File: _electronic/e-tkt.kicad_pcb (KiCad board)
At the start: 4 copper layers, 99.6 x 76.2 mm, 110 parts

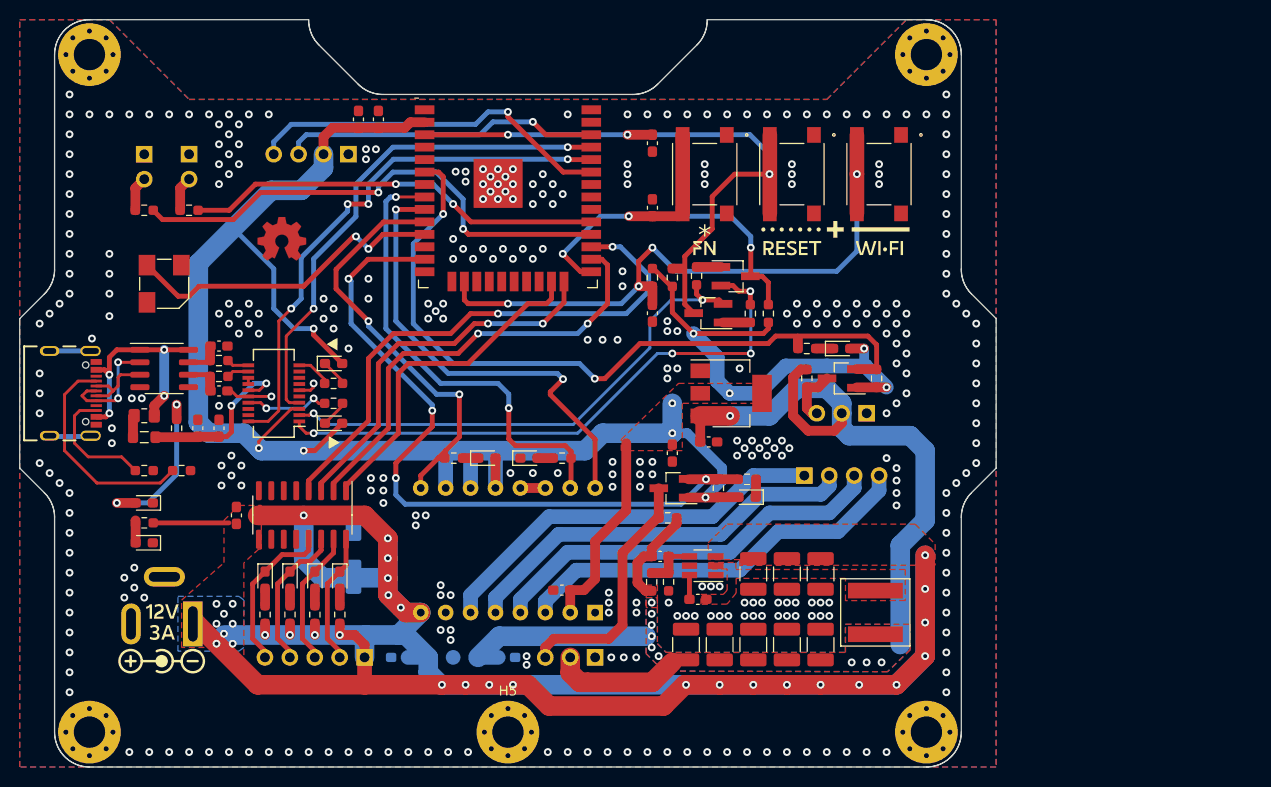
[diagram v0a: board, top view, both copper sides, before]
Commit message: BETA first upload
nothing major done here:
* updated KiCAD files to v9
* removed alternative 6v feed-in. The proposed buck converter is fine.
* added to all components LCSC component IDs. With this, exporting the project as gerber files also automatically creates correct BOM for JLCPCB manufacturing
*
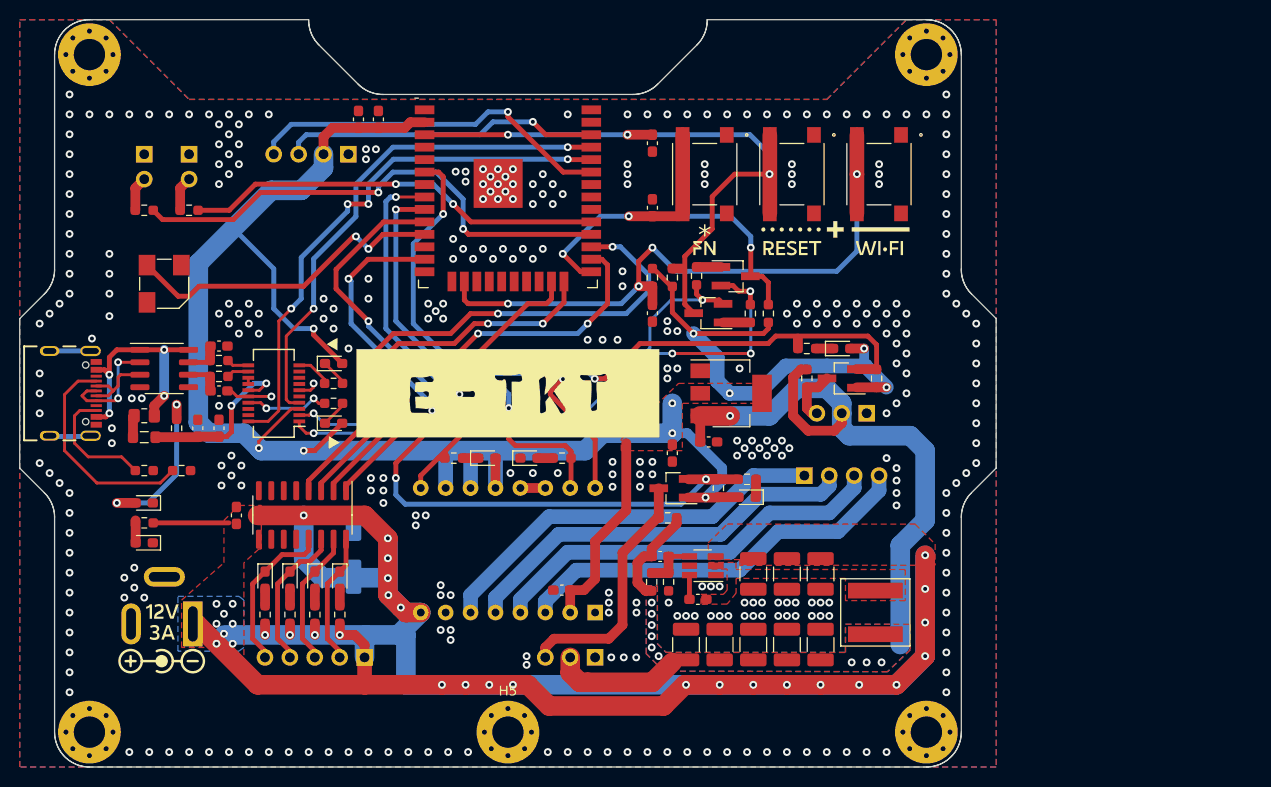
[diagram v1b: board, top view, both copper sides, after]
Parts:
- removed C_ALT6V_1: 0.33uF 50V, Capacitor_SMD:C_0603_1608Metric_Pad1.08x0.95mm_HandSolder
- removed C_ALT6V_2: 0.1uF 50V, Capacitor_SMD:C_0603_1608Metric_Pad1.08x0.95mm_HandSolder
- removed J_12v_ALT6V1, J_6v_ALT6V1, J_GND_ALT6V1: TestPoint, TestPoint:TestPoint_Pad_D1.5mm
- removed REF**: OSHW-Symbol_6.7x6mm_SilkScreen, andrei custom:opengear_small
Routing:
- net +6V: track 108.1 -> 88.0 mm

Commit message: Added CAD, cleaned up KiCAD some more
Added a FreeCAD Assembly. This will serve for minor updated to the printable parts.
Updated USB-C component to standard KiCAD libary-integrated version, because the pinout of the schematic symbol was messing with the pinout of the footprint
exported the PCB as step so it could be imported to FreeCAD
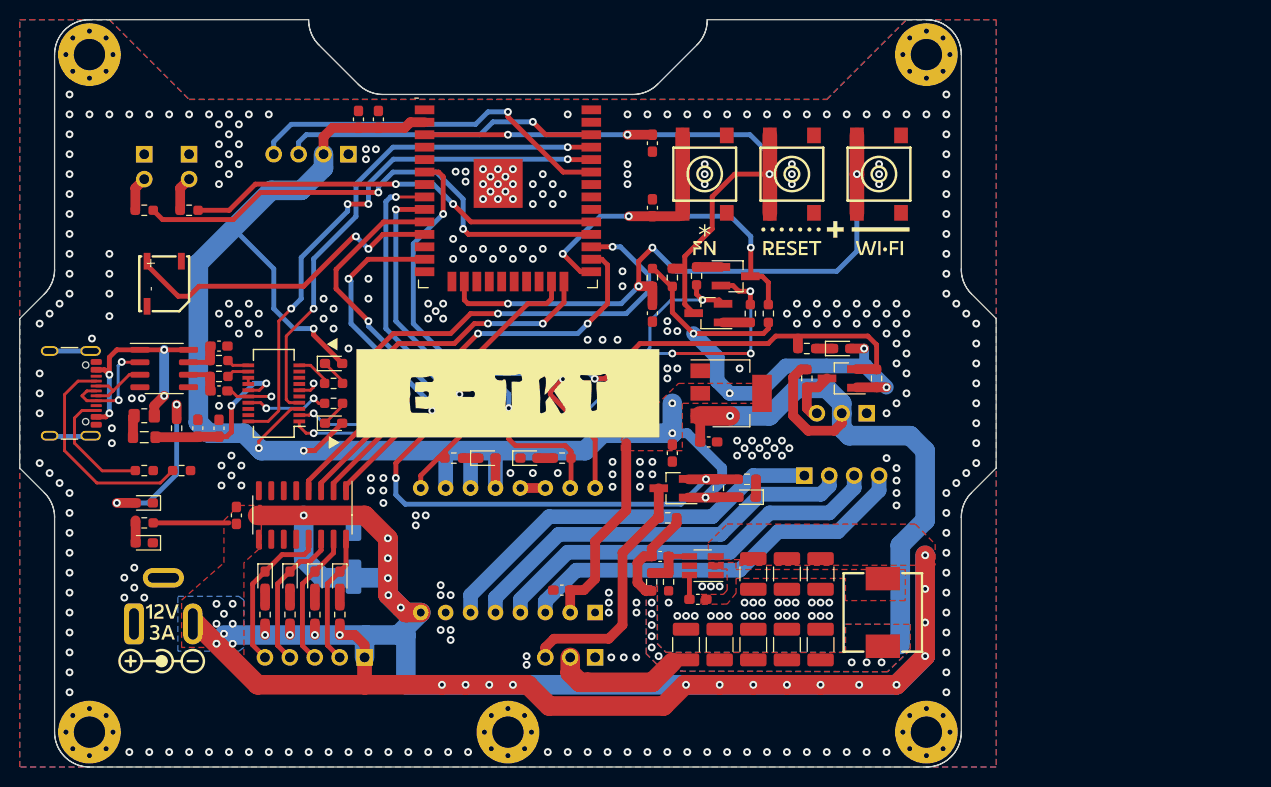
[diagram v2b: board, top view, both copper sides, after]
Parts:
- J_POW1: footprint SnapEDA Library:BarrelJack_GCT_DCJ200-10-A_Horizontal -> EASYEDA2KICAD:BarrelJack_Horizontal
- J_USB1: value USB4105-GF-A -> USB_C_Receptacle_USB2.0_16P; footprint SnapEDA Library:GCT_USB4105-GF-A -> Connector_USB:USB_C_Receptacle_GCT_USB4105-xx-A_16P_TopMnt_Horizontal
- L1: footprint SRP6060FA:SRP6060FA-4R7M -> EASYEDA2KICAD:IND-SMD_L8.5-W8.0_PSPMAA0803H-330M-ANP
- LS1: footprint SnapEDA Library:CUI_CSS-0575A-SMT -> EASYEDA2KICAD:BUZ-SMD_L5.0-W5.5-P4.60
- SW_DFU1, SW_ENA1, SW_WIFI1: footprint b3fs:B3FS-1000 -> EASYEDA2KICAD:KEY-SMD_4P-L6.0-W6.3-P4.50-LS8.0
- moved J_USB1 1.07 mm to (132.6, -189.5)
- moved L1 0.76 mm to (216.5, -167.1)
- turned J_POW1 to 0 degrees
- turned SW_DFU1 to 90 degrees
- turned SW_ENA1 to 90 degrees
- turned SW_WIFI1 to 90 degrees
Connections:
- net /USB-C 2.0/USBD1+ renamed Net-(J_USB1-D+-PadA6)
- net /USB-C 2.0/USBD1- renamed Net-(J_USB1-D--PadA7)
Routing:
- net Net-(J_USB1-D--PadA7): track 7.09 -> 6.57 mm

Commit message: Updated A_bottom in FreeCAD
added pockets for M3 nuts, added pockets for electronics cover

started to optimize pcb footprint layout and voltage reference planes
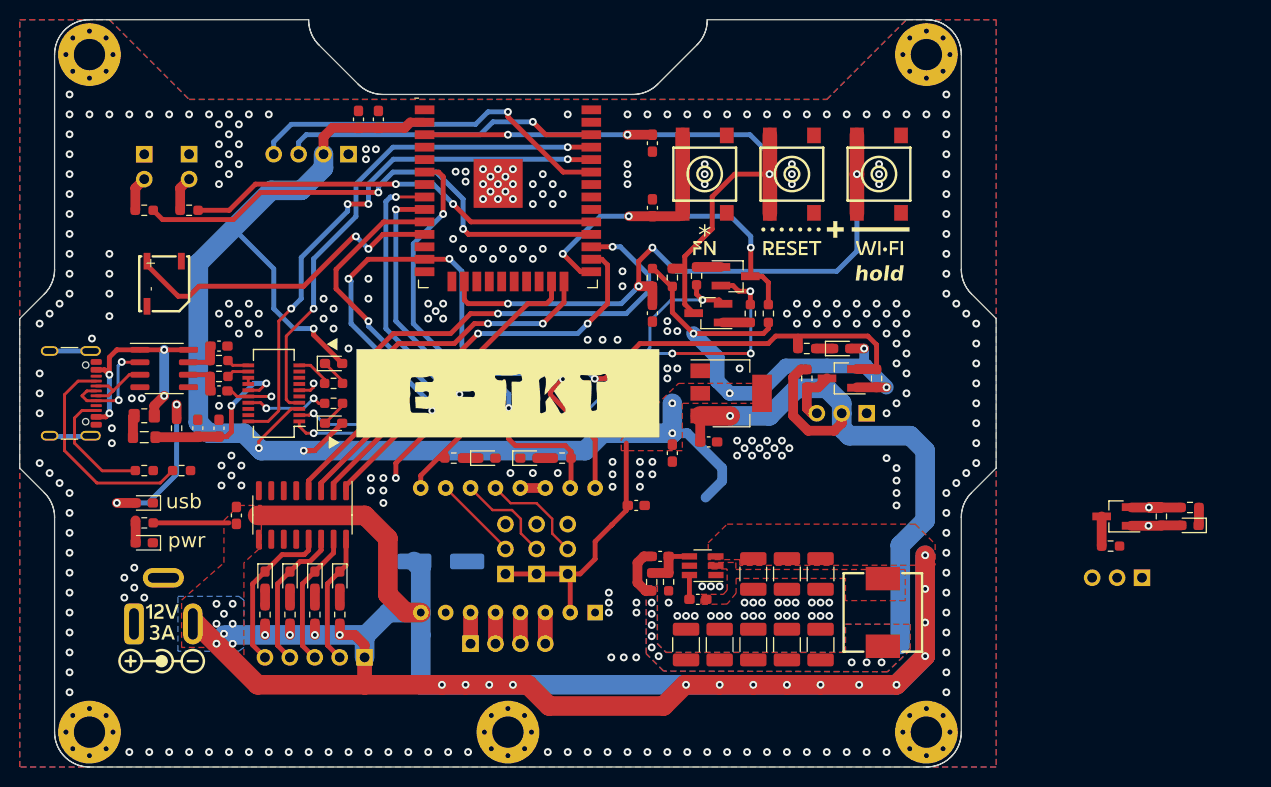
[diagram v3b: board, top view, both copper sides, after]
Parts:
- added J1: Conn_01x03_Pin, Connector_PinHeader_2.54mm:PinHeader_1x03_P2.54mm_Vertical, B.Cu at (178.1, -171.1)
- added J2: Conn_01x03_Pin, Connector_PinHeader_2.54mm:PinHeader_1x03_P2.54mm_Vertical, B.Cu at (181.2, -171.1)
- added J3: Conn_01x03_Pin, Connector_PinHeader_2.54mm:PinHeader_1x03_P2.54mm_Vertical, B.Cu at (184.4, -171.1)
- J_NEMA1: footprint Connector_PinHeader_2.54mm:PinHeader_1x04_P2.54mm_Horizontal -> Connector_PinHeader_2.54mm:PinHeader_1x04_P2.54mm_Vertical
- moved J_SERVO1 56.4 mm to (243.0, -170.7)
- moved Q_SERVO1 45.3 mm to (240.4, -176.9)
- moved R_SERVO2 45.3 mm to (244.9, -176.9)
- moved D_SERVO1 45.3 mm to (247.9, -176.0)
- moved R_SERVO1 45.3 mm to (239.8, -173.9)
- moved R_SERVO3 45.3 mm to (247.9, -177.8)
- moved G*** 41.0 mm to (152.6, -221.2)
- moved J_NEMA1 38.1 mm to (174.5, -164.0)
- moved C_NEMA2 11.5 mm to (191.4, -178.1), turned to 180 degrees
- moved C_NEMA1 8.96 mm to (171.4, -172.3), turned to 0 degrees
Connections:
- A_NEMA1 pad 10: +3.3V -> Net-(A_NEMA1-MS1)
- A_NEMA1 pad 11: +3.3V -> Net-(A_NEMA1-MS2)
- A_NEMA1 pad 12: +3.3V -> Net-(A_NEMA1-MS3)
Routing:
- net Net-(A_NEMA1-1B): track 41.4 -> 3.18 mm
- net Net-(A_NEMA1-1A): track 41.3 -> 3.18 mm
- net Net-(A_NEMA1-2A): track 41.3 -> 3.18 mm
- net Net-(A_NEMA1-2B): track 40.9 -> 3.18 mm
- net IO14 SERVO: track 76.4 -> 53.5 mm, vias 4 -> 5
- net SERVO: track 25.4 -> 3.02 mm
- net +6V: track 88.0 -> 69.8 mm
- net +12V: track 251.2 -> 233.2 mm, vias 33 -> 27
- net Net-(A_NEMA1-MS3): track 0.00 -> 10.8 mm
- net Net-(A_NEMA1-MS2): track 0.00 -> 10.2 mm
- net Net-(A_NEMA1-MS1): track 0.00 -> 8.76 mm
- net +3.3V: track 231.2 -> 223.3 mm
- net GNDREF: vias 351 -> 339
- added copper zone on In2.Cu, net +3.3V
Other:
- board text added: "H"
- board text added: "L"
- board text added: "hold"
- board text added: "pwr"
- board text added: "usb"

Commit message: Minor adjustments of CAD and EDA
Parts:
- moved J_SERVO1 26.8 mm to (253.3, -195.4)
- moved R_WIFI1 23.0 mm to (211.6, -214.8), turned to -90 degrees
- moved C_WIFI1 21.6 mm to (211.6, -208.7), turned to -90 degrees
- moved R_SERVO1 21.0 mm to (251.0, -191.6), turned to 90 degrees
- moved R_DFU1 20.4 mm to (194.0, -214.9)
- moved D_SERVO1 20.1 mm to (244.5, -195.8), turned to 0 degrees
- moved R_SERVO2 17.3 mm to (244.5, -194.2), turned to 0 degrees
- moved Q_SERVO1 16.3 mm to (247.4, -191.6), turned to 0 degrees
- moved Q_HALL1 16.0 mm to (196.4, -191.4)
- moved R_HALL2 15.9 mm to (200.0, -191.4)
- moved R_ENA1 15.6 mm to (202.8, -214.8)
- moved R_SERVO3 14.4 mm to (243.6, -191.6), turned to -90 degrees
- moved R_HALL1 14.4 mm to (194.9, -187.4), turned to -90 degrees
- moved U_POW2 14.0 mm to (190.5, -180.3), turned to 90 degrees
- moved J_HALL1 11.9 mm to (202.9, -187.4)
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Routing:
- net +3.3V: track 223.3 -> 120.0 mm, vias 10 -> 13
- net +6V: track 69.8 -> 13.1 mm, vias 10 -> 17
- net IO34 HALL: track 75.9 -> 42.6 mm
- net IO14 SERVO: track 53.5 -> 37.5 mm, vias 5 -> 3
- net +12V: track 233.2 -> 227.7 mm, vias 27 -> 20
- net IO32 NEMA STEP: track 47.6 -> 42.7 mm
- net GNDREF: track 15.1 -> 19.3 mm, vias 339 -> 286
- net EN: track 69.7 -> 65.8 mm, vias 3 -> 2
- net DTR: track 61.0 -> 57.4 mm, vias 4 -> 2
- net SERVO: track 3.02 -> 0.00 mm
- net IO25 NEMA ENA: track 43.0 -> 45.8 mm
- net IO33 NEMA DIR: track 47.4 -> 45.4 mm
- net Net-(D_SERVO1-K): track 1.84 -> 0.00 mm
- net IO0 DFU: track 47.3 -> 45.6 mm
- net IO13 WIFI RST: track 66.9 -> 68.3 mm
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- removed copper zone on F.Cu, net +3.3V

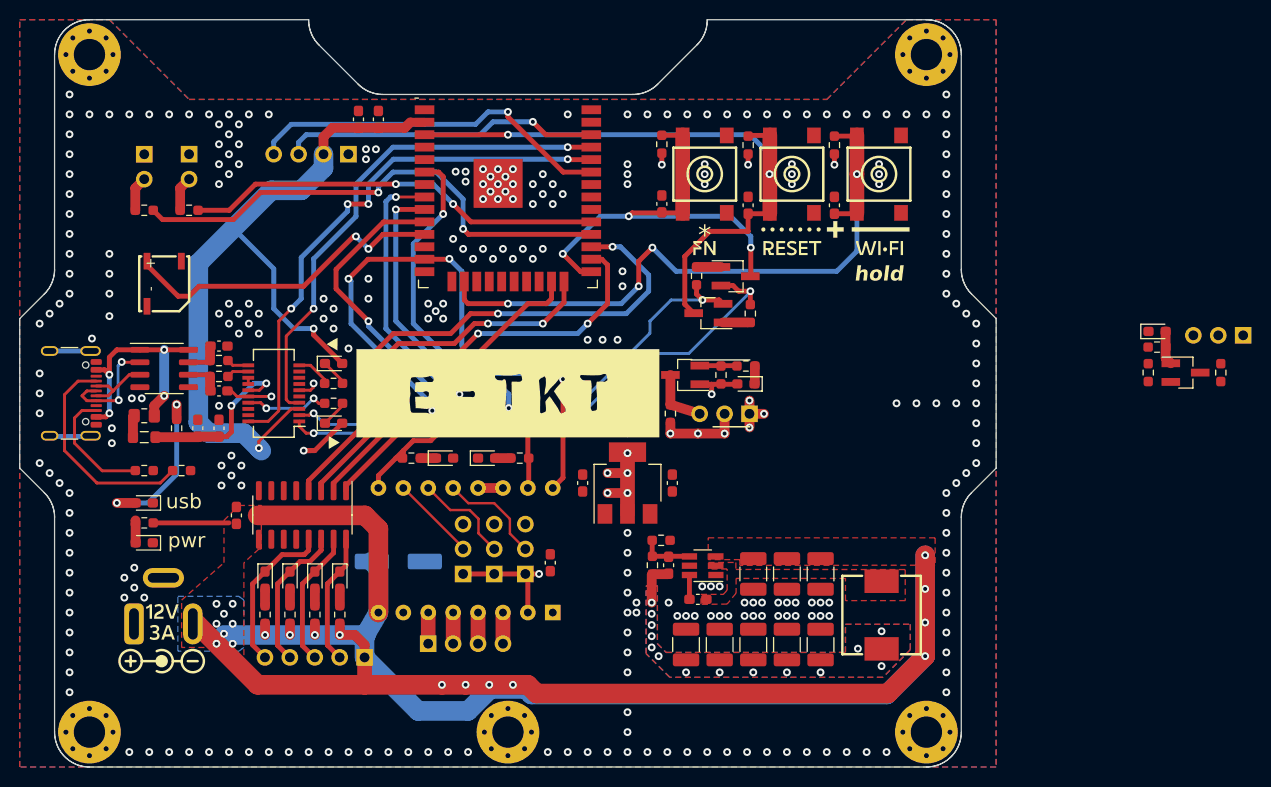
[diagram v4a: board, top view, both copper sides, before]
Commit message: Updating KiCAD files
some footprints in KicCAD v9 were updated versus v6 and threw warnings/errors. All footprints are now v9 compatible
wiring from ESP32 pins was optimized
layout of servo and hall level shift was optimized
layer 3 was split in 6V plane around the DCDC and 3V3 plane around everywhere else
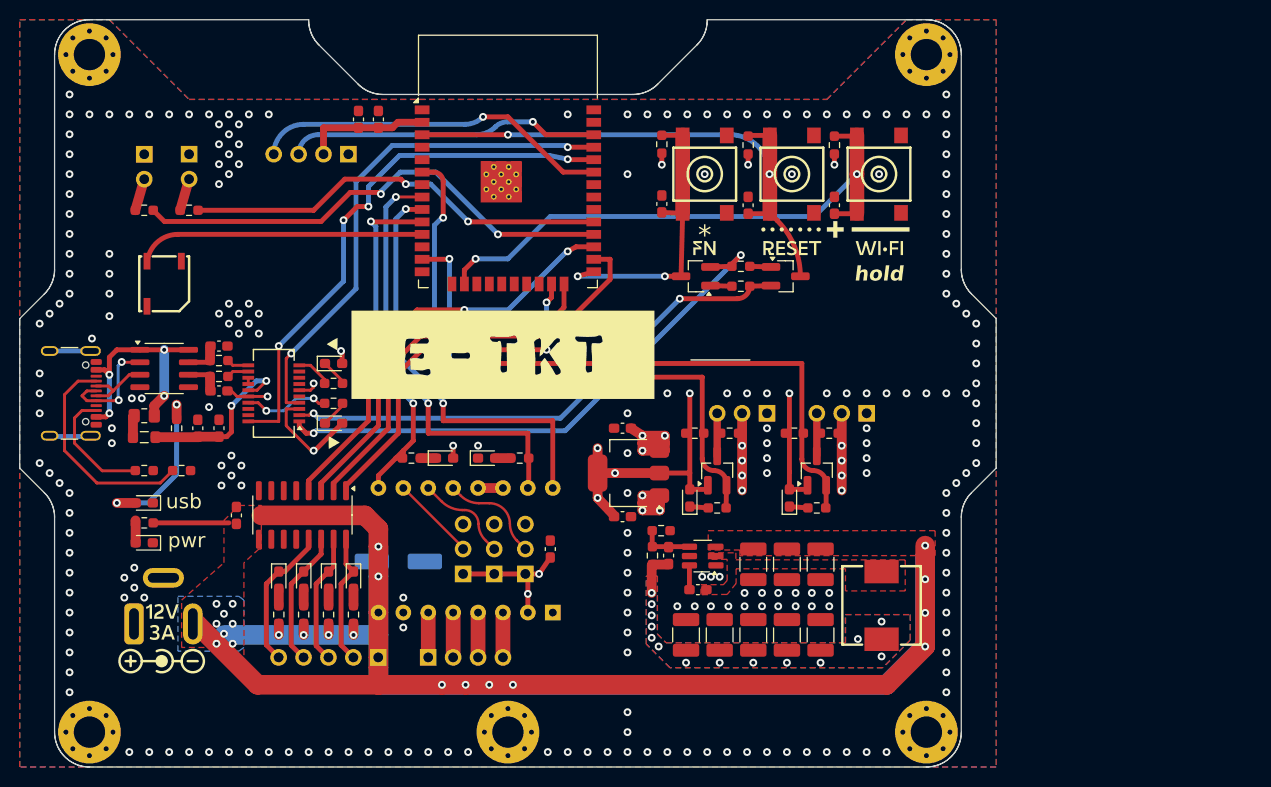
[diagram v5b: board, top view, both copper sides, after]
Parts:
- moved D_SERVO1 50.6 mm to (196.8, -178.8), turned to 90 degrees
- moved R_SERVO1 50.5 mm to (200.9, -185.4), turned to 0 degrees
- moved J_SERVO1 49.2 mm to (204.7, -187.5)
- moved Q_SERVO1 48.8 mm to (199.6, -181.6), turned to 90 degrees
- moved R_SERVO2 48.0 mm to (197.4, -185.4), turned to 180 degrees
- moved R_SERVO3 46.1 mm to (199.6, -177.8), turned to 180 degrees
- moved G*** 17.4 mm to (180.6, -206.2)
- moved Q_HALL1 16.6 mm to (209.8, -181.6), turned to 90 degrees
- moved R_HALL1 16.3 mm to (211.1, -185.4), turned to 0 degrees
- moved R_HALL3 16.2 mm to (209.8, -177.8), turned to 180 degrees
- moved D_HALL1 12.4 mm to (207.0, -178.8), turned to 90 degrees
- moved J_HALL1 11.9 mm to (214.9, -187.5)
- moved R_HALL2 9.55 mm to (207.5, -185.4), turned to 180 degrees
- moved Q_AUTO1 8.73 mm to (206.6, -201.4), turned to 0 degrees
- moved C_POW1 7.55 mm to (190.0, -185.9), turned to 180 degrees
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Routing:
- net +3.3V: track 120.0 -> 83.8 mm
- net IO34 HALL: track 42.6 -> 75.2 mm
- net +6V: track 13.1 -> 31.5 mm, vias 17 -> 25
- net IO14 SERVO: track 37.5 -> 55.0 mm, vias 3 -> 2
- net IO0 DFU: track 45.6 -> 31.4 mm, vias 3 -> 2
- net IO16 ULN 4: track 56.1 -> 43.4 mm
- net IO13 WIFI RST: track 68.3 -> 57.9 mm, vias 4 -> 2
- net EN: track 65.8 -> 56.9 mm
- net IO25 NEMA ENA: track 45.8 -> 37.4 mm
- net SERVO: track 0.00 -> 4.34 mm
- net GNDREF: track 19.3 -> 23.1 mm, vias 286 -> 233
- net /MCU/IO26 BUZZER OUT: track 33.3 -> 30.0 mm, vias 2 -> 0
- net IO15 ULN 1: track 34.7 -> 37.4 mm, vias 0 -> 2
- net RTS: track 51.6 -> 54.1 mm
- net IO32 NEMA STEP: track 42.7 -> 44.9 mm
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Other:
- board text removed: "6V"
- board text removed: "IN"
